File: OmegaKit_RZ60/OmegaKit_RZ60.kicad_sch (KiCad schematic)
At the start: 27 parts, among them SW1 SW_CK_OS102011MS2Q, U1 AMS1117-5.0

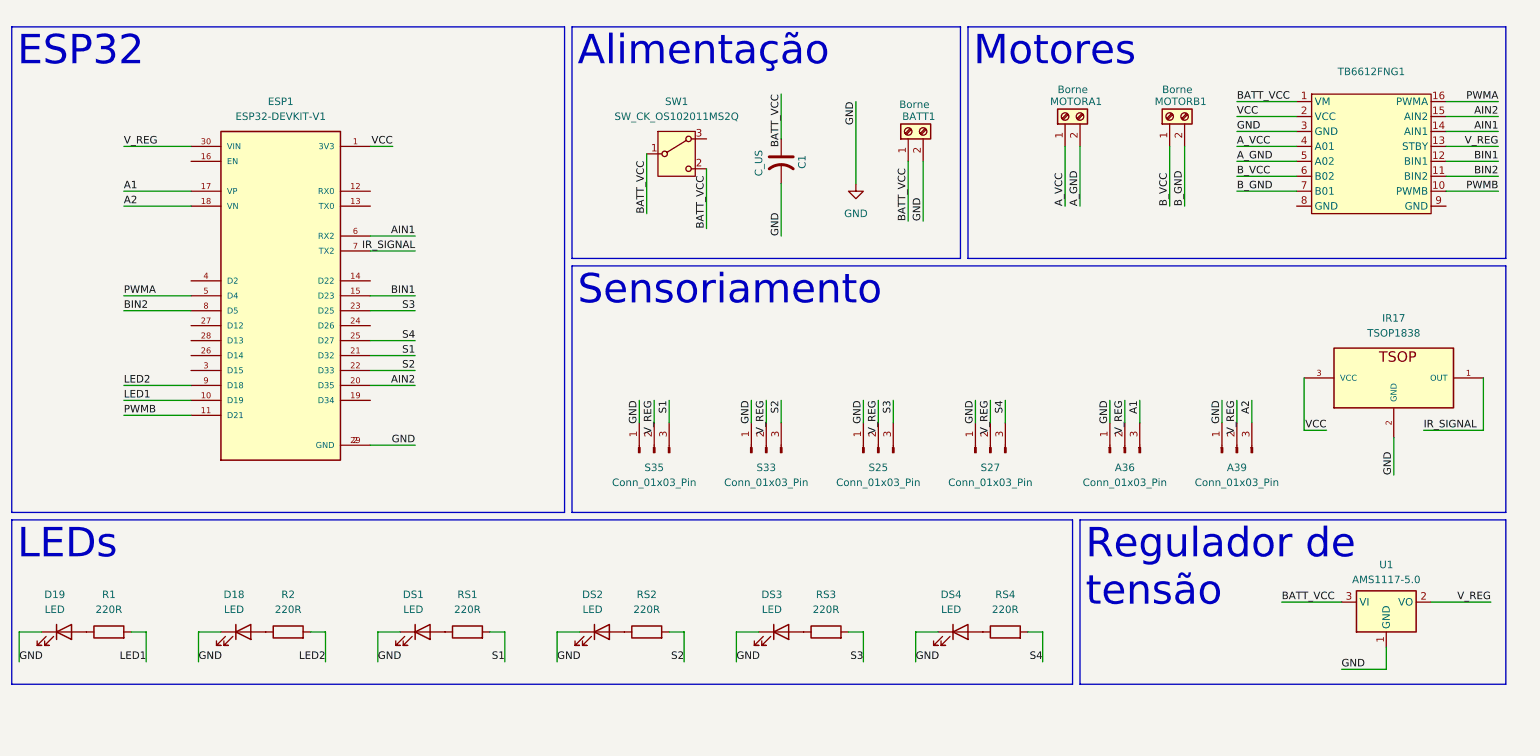
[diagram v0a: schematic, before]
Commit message: Correção de pinos + novas plotagens + modelos step + gerbers
Co-authored-by: rarolle <rarolle@gmail.com>
Co-authored-by: RafaHR <rafahramos02@gmail.com>
Co-authored-by: Guilherme36 <guilherminhofeh@hotmail.com>
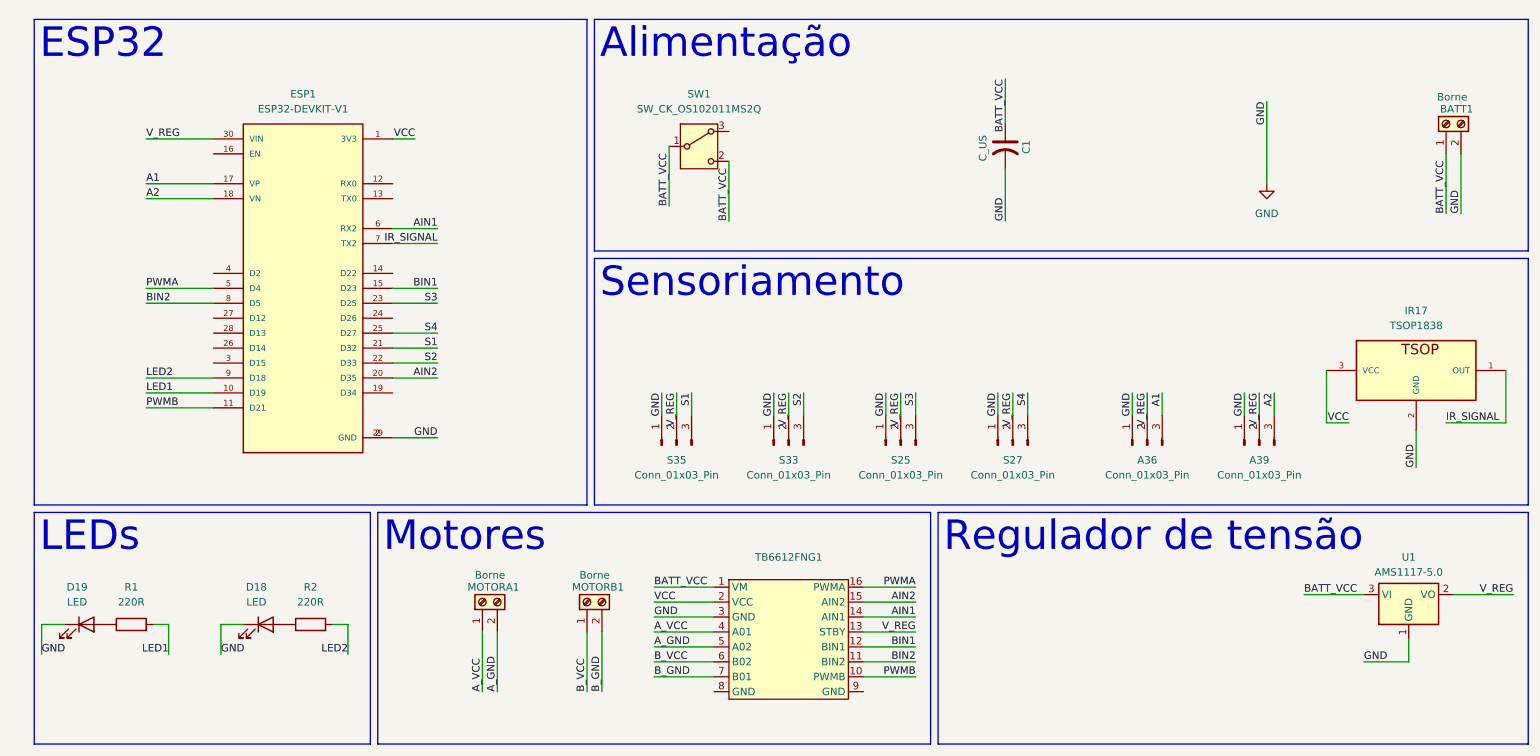
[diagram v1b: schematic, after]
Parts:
- removed DS1, DS2, DS3, DS4: LED, LED_SMD:LED_0603_1608Metric, symbol Device:LED
- removed RS1, RS2, RS3, RS4: 220R, Resistor_SMD:R_0603_1608Metric, symbol Device:R
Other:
- moved on the sheet: A36, A39, BATT1, C1, D18, D19, ESP1, IR17, MOTORA1, MOTORB1, R1, R2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
